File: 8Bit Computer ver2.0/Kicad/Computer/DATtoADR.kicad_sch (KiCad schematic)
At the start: 12 parts, among them IC224 SN74F521DWR, IC225 SN74F521DWR, IC226 SN74F521DWR, IC227 SN74LVC1G14DBVR, IC228 SN74LVC1G14DBVR, IC229 SN74LVC1G14DBVR, IC230 SN74LVC1G14DBVR, IC231 SN74ABT574ADWR, IC232 SN74ABT574ADWR, IC233 SN74AHC74DR, IC234 SN74ABT245BDWR, IC235 SN74ABT245BDWR

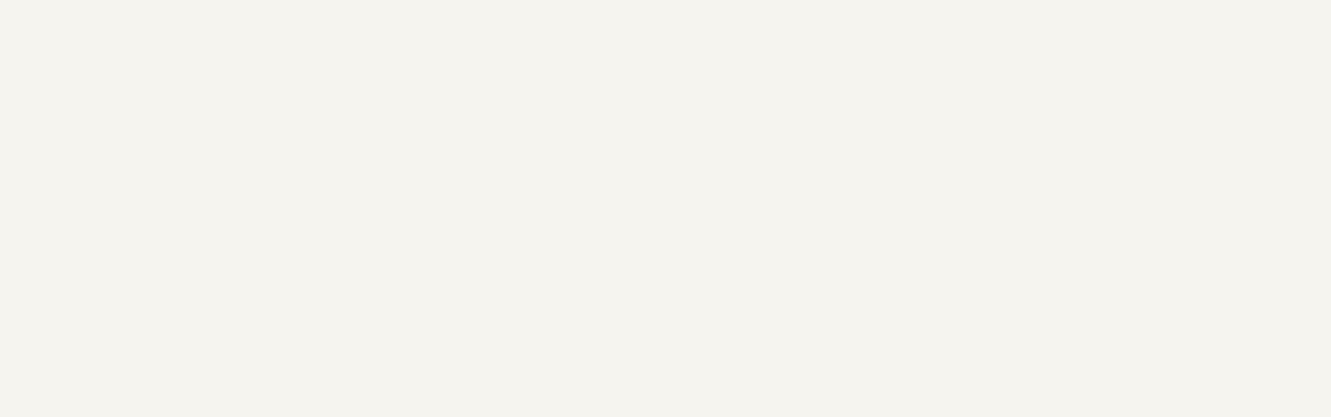
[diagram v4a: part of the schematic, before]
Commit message: Kicad
added the Programme Counter und Dat to adr module
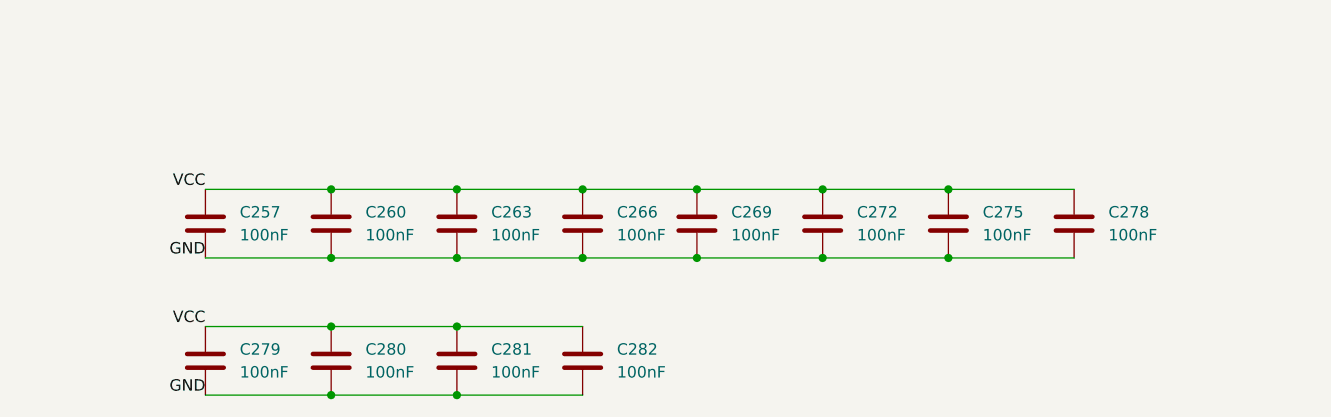
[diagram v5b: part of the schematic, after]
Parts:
- added C257, C260, C263, C266, C269, C272, C275, C278, C279, C280, C281, C282: 100nF, Capacitor_SMD:C_1206_3216Metric_Pad1.33x1.80mm_HandSolder, symbol Device:C
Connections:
- net GND: now also C257.1, C260.1, C263.1, C266.1, C269.1, C272.1, C275.1, C278.1, C279.1, C280.1, C281.1, C282.1
- net VCC: now also C257.2, C260.2, C263.2, C266.2, C269.2, C272.2, C275.2, C278.2, C279.2, C280.2, C281.2, C282.2

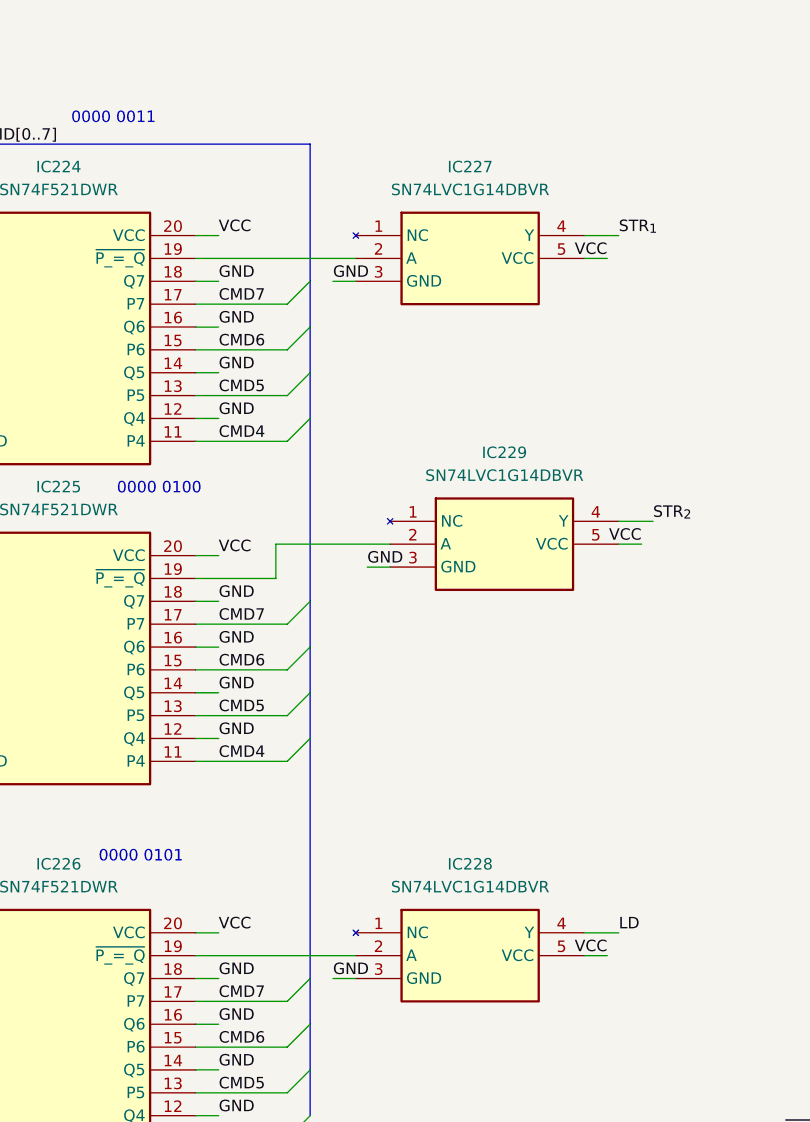
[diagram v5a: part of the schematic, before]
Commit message: Kicad
added 10pin 2,54mm Header
finished ALU PCB and added pin Header for extra use (DAT,ADR,CMD,Ddis,CLK)
31.12-06.01 about +60hr for ALU
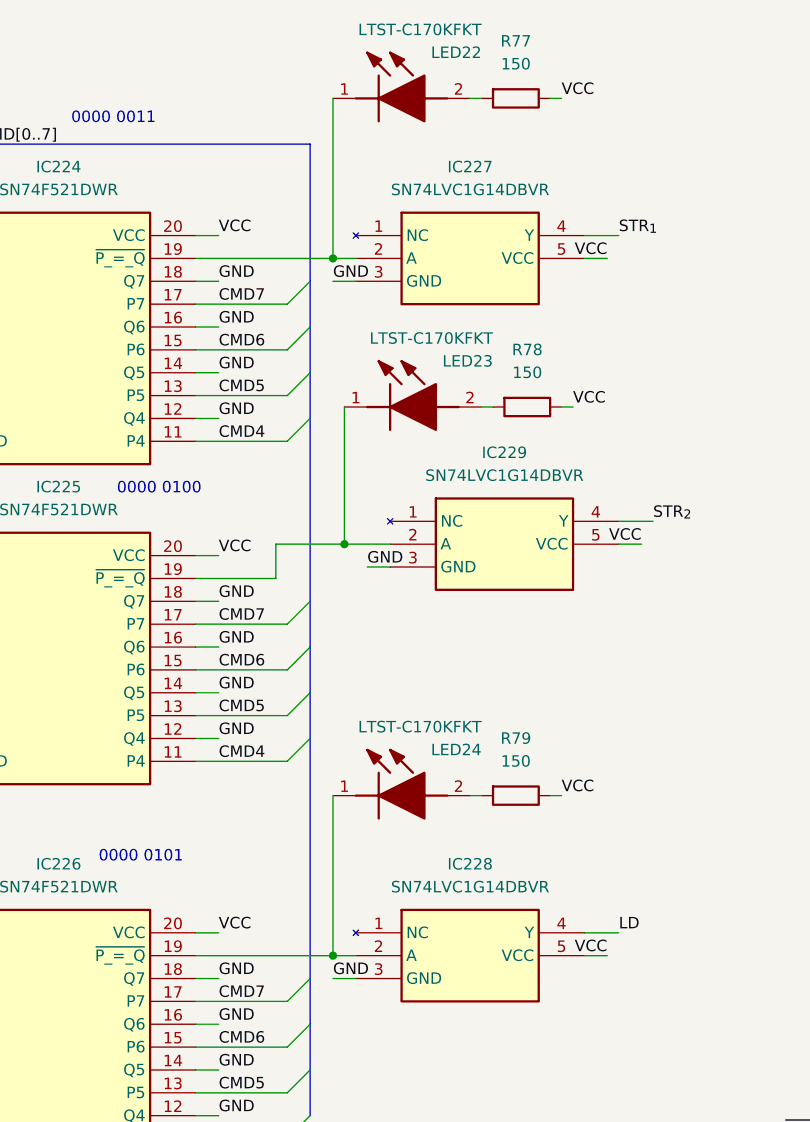
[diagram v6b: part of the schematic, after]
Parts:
- added LED22, LED23, LED24: LTST-C170KFKT, Samacsys:LEDC2012X120N, symbol Samacsys:LTST-C170KFKT
- added R77, R78, R79: 150, Resistor_SMD:R_1206_3216Metric_Pad1.30x1.75mm_HandSolder, symbol Device:R
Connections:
- net VCC: now also R77.1, R78.1, R79.1
- net at IC224.19 (~{P_=_Q}), IC227.2 (A): now also LED22.1 (K)
- net at IC226.19 (~{P_=_Q}), IC228.2 (A): now also LED24.1 (K)
- net at IC225.19 (~{P_=_Q}), IC229.2 (A): now also LED23.1 (K)
- new net: LED23.2 (A), R78.2
- new net: LED24.2 (A), R79.2
- new net: LED22.2 (A), R77.2

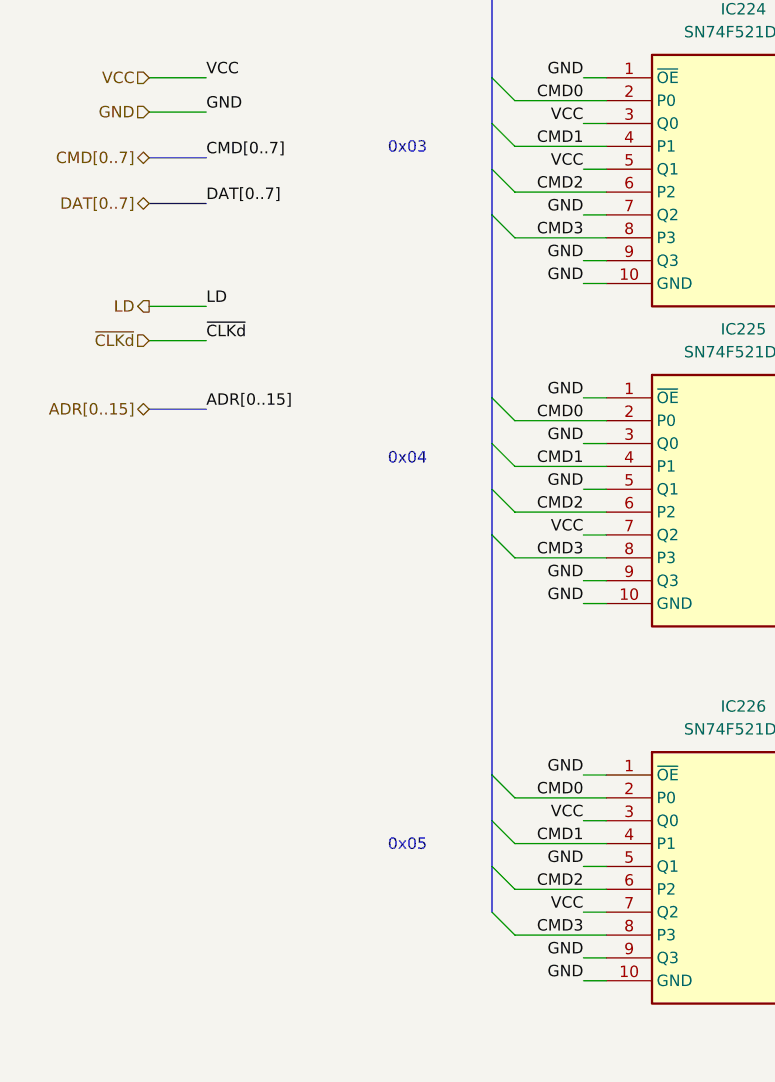
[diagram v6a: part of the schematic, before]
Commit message: Kicad
fixed some design errors(dat dis DistShiftreg, wrong cmd pins)
added description to every CMD for better debug, use CTRL+f and use option "Whole words only" to search e.g. inc
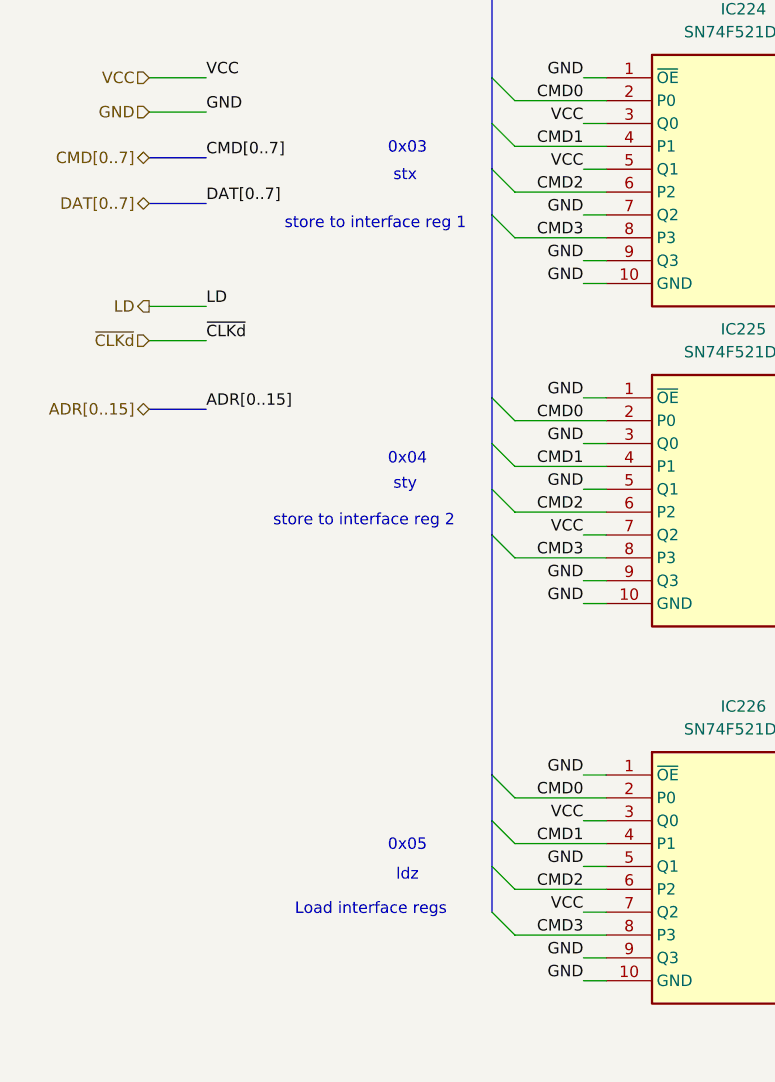
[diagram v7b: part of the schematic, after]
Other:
- note added: "Load interface regs"
- note added: "ldz"
- note added: "store to interface reg 1"
- note added: "store to interface reg 2"
- note added: "stx"
- note added: "sty"
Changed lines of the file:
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@@
+		)
+	)
+	(text "sty"
+		(exclude_from_sim no)
+		(at 64.008 83.312 0)
+		(effects
+			(font
+				(size 1.27 1.27)
+			)
+		)
+	)
+	(text "ldz"
+		(exclude_from_sim no)
+		(at 64.262 126.746 0)
+		(effects
+			(font
+				(size 1.27 1.27)
+			)
 		)
 	)
@@
 		(exclude_from_sim no)
 		(at 112.776 66.294 0)
+		(effects
+			(font
+				(size 1.27 1.27)
+			)
+		)
+	)
+	(text "stx"
+		(exclude_from_sim no)
+		(at 64.008 49.022 0)
 		(effects
 			(font
@@
 		)
 	)
+	(text "store to interface reg 2"
+		(exclude_from_sim no)
+		(at 59.436 87.376 0)
+		(effects
+			(font
+				(size 1.27 1.27)
+			)
+		)
+	)
+	(text "store to interface reg 1"
+		(exclude_from_sim no)
+		(at 60.706 54.356 0)
+		(effects
+			(font
+				(size 1.27 1.27)
+			)
+		)
+	)
 	(text "0x03\n\n"
 		(exclude_from_sim no)
@@
 		(effects
 			(font
+				(size 1.27 1.27)
+			)
+		)
+	)
+	(text "Load interface regs"
+		(exclude_from_sim no)
+		(at 60.198 130.556 0)
+		(effects
+			(font

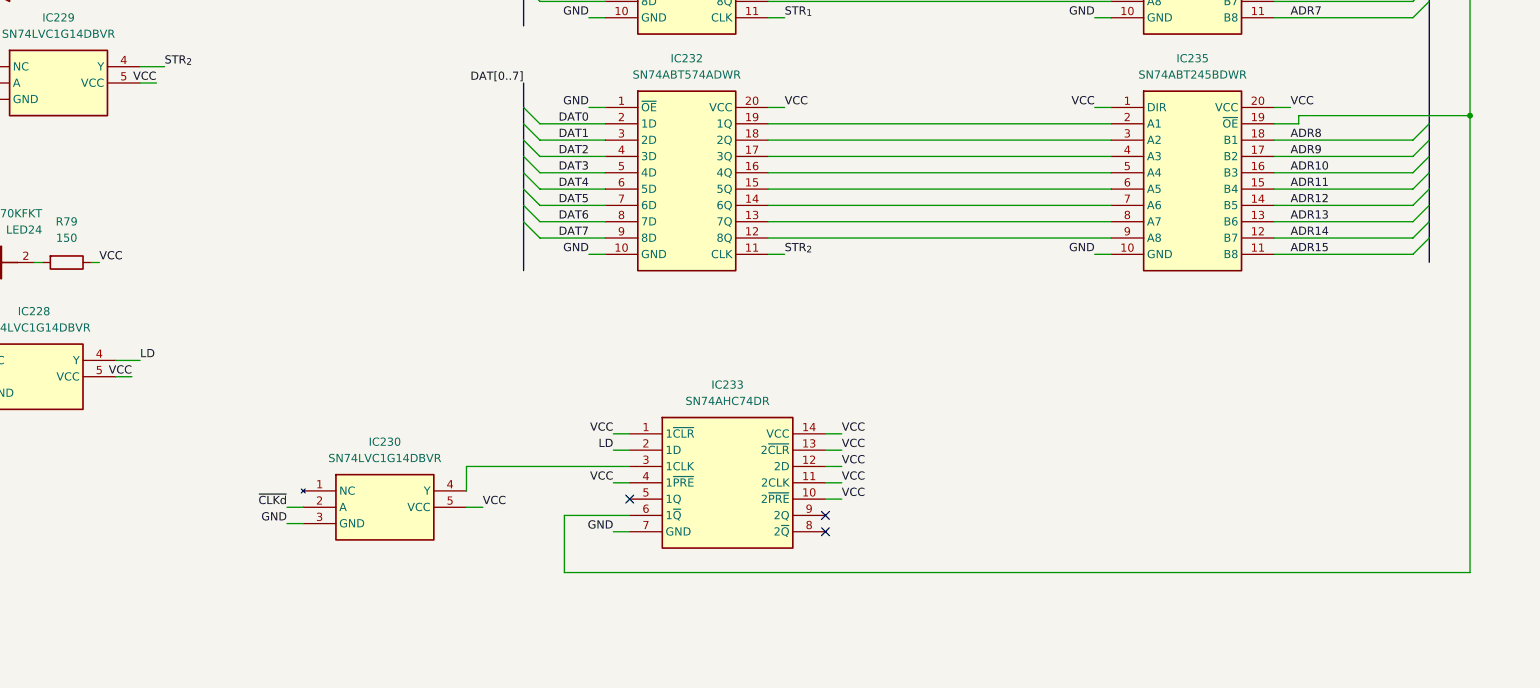
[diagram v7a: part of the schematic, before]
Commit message: fixes
fixed timing for dat to adr register
added a new short test programme for dat to adr register
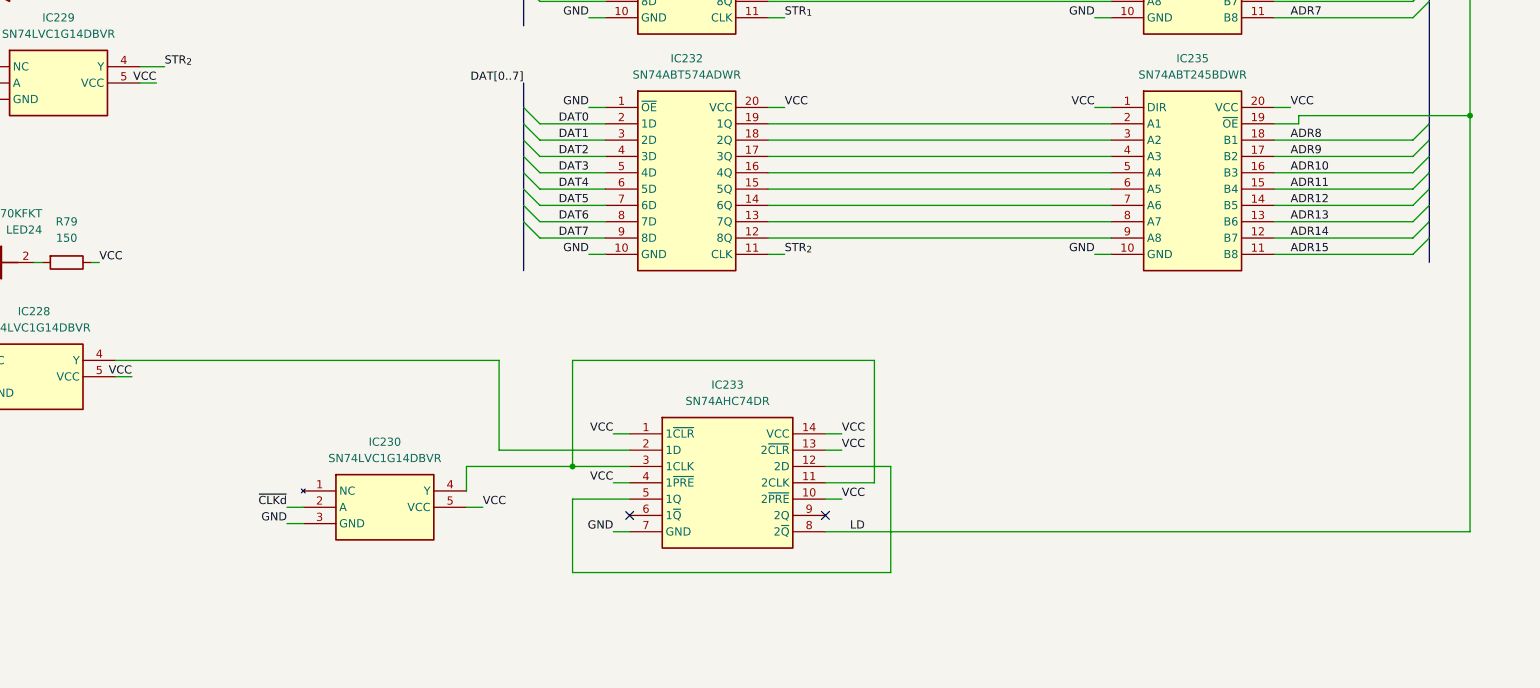
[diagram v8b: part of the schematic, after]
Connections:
- net LD: now also IC233.8 (2~{Q}), IC234.19 (~{OE}), IC235.19 (~{OE}); no longer IC228.4 (Y), IC233.2 (1D)
- net VCC: no longer IC233.11 (2CLK), IC233.12 (2D)
- net at IC230.4 (Y), IC233.3 (1CLK): now also IC233.11 (2CLK)
- net at IC233.5 (1Q): now also IC233.12 (2D)
- new net: IC228.4 (Y), IC233.2 (1D)
- now unconnected: IC233.6 (1~{Q})
- no-connect marks 3 -> 2
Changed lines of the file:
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@@
 	)
 	(junction
+		(at 231.14 132.08)
+		(diameter 0)
+		(color 0 0 0 0)
+	)
+	(junction
 		(at 199.39 179.07)
 		(diameter 0)
@@
 	)
 	(no_connect
-		(at 270.51 139.7)
-	)
-	(no_connect
-		(at 240.03 137.16)
+		(at 240.03 139.7)
 	)
 	(no_connect
-		(at 270.51 142.24)
+		(at 270.51 139.7)
 	)
 	(bus_entry
@@
 	(wire
 		(pts
+			(xy 278.13 134.62) (xy 278.13 115.57)
+		)
+		(stroke
+			(width 0)
+			(type default)
+		)
+	)
+	(wire
+		(pts
 			(xy 340.36 83.82) (xy 361.95 83.82)
 		)
@@
 	(wire
 		(pts
-			(xy 160.02 115.57) (xy 163.83 115.57)
-		)
-		(stroke
-			(width 0)
-			(type default)
-		)
-	)
-	(wire
-		(pts
 			(xy 119.38 120.65) (xy 116.84 120.65)
 		)
@@
 		)
 	)
-	(wire
-		(pts
-			(xy 237.49 129.54) (xy 240.03 129.54)
-		)
-		(stroke
-			(width 0)
-			(type default)
-		)
-	)
 	(bus
 		(pts
@@
 	(wire
 		(pts
-			(xy 370.84 148.59) (xy 370.84 77.47)
+			(xy 370.84 142.24) (xy 370.84 77.47)
 		)
 		(stroke
@@
 	(wire
 		(pts
-			(xy 270.51 134.62) (xy 273.05 134.62)
+			(xy 270.51 134.62) (xy 278.13 134.62)
 		)
 		(stroke
@@
 	(wire
 		(pts
-			(xy 229.87 139.7) (xy 229.87 148.59)
-		)
-		(stroke
-			(width 0)
-			(type default)
-		)
-	)
-	(wire
-		(pts
 			(xy 76.2 123.19) (xy 86.36 123.19)
 		)
@@
 	(wire
 		(pts
+			(xy 278.13 115.57) (xy 231.14 115.57)
+		)
+		(stroke
+			(width 0)
+			(type default)
+		)
+	)
+	(wire
+		(pts
 			(xy 158.75 171.45) (xy 172.72 171.45)
 		)
@@
 	(wire
 		(pts
-			(xy 214.63 132.08) (xy 240.03 132.08)
+			(xy 214.63 132.08) (xy 231.14 132.08)
 		)
 		(stroke
@@
 	(wire
 		(pts
+			(xy 270.51 142.24) (xy 370.84 142.24)
+		)
+		(stroke
+			(width 0)
+			(type default)
+		)
+	)
+	(wire
+		(pts
 			(xy 199.39 179.07) (xy 213.36 179.07)
 		)
@@
 	(wire
 		(pts
+			(xy 160.02 115.57) (xy 219.71 115.57)
+		)
+		(stroke
+			(width 0)
+			(type default)
+		)
+	)
+	(wire
+		(pts
 			(xy 261.62 54.61) (xy 314.96 54.61)
 		)
@@
 		)
 	)
+	(wire
+		(pts
+			(xy 231.14 132.08) (xy 240.03 132.08)
+		)
+		(stroke
+			(width 0)
+			(type default)
+		)
+	)
 	(bus
 		(pts
@@
 	(wire
 		(pts
+			(xy 231.14 115.57) (xy 231.14 132.08)
+		)
+		(stroke
+			(width 0)
+			(type default)
+		)
+	)
+	(wire
+		(pts
 			(xy 148.59 100.33) (xy 147.32 100.33)
 		)
@@
 	(wire
 		(pts
+			(xy 219.71 129.54) (xy 219.71 115.57)
+		)
+		(stroke
+			(width 0)
+			(type default)
+		)
+	)
+	(wire
+		(pts
 			(xy 158.75 186.69) (xy 172.72 186.69)
 		)
@@
 		)
 	)
+	(wire
+		(pts
+			(xy 280.67 132.08) (xy 270.51 132.08)
+		)
+		(stroke
+			(width 0)
+			(type default)
+		)
+	)
 	(bus
 		(pts
@@
 	(wire
 		(pts
-			(xy 240.03 139.7) (xy 229.87 139.7)
-		)
-		(stroke
-			(width 0)
-			(type default)
-		)
-	)
-	(wire
-		(pts
 			(xy 156.21 22.86) (xy 157.48 22.86)
 		)
@@
 		)
 	)
-	(wire
-		(pts
-			(xy 270.51 132.08) (xy 273.05 132.08)
-		)
-		(stroke
-			(width 0)
-			(type default)
-		)
-	)
 	(bus
 		(pts
@@
 		)
 	)
-	(bus
+	(wire
 		(pts
-			(xy 223.52 54.61) (xy 223.52 57.15)
+			(xy 240.03 137.16) (xy 231.14 137.16)
 		)
 		(stroke
@@
 		)
 	)
-	(wire
+	(bus
 		(pts
-			(xy 229.87 148.59) (xy 370.84 148.59)
+			(xy 223.52 54.61) (xy 223.52 57.15)
 		)
 		(stroke
@@
 	(wire
 		(pts
+			(xy 280.67 148.59) (xy 280.67 132.08)
+		)
+		(stroke
+			(width 0)
+			(type default)
+		)
+	)
+	(wire
+		(pts
 			(xy 119.38 58.42) (xy 116.84 58.42)
 		)
@@
 	(wire
 		(pts
+			(xy 231.14 148.59) (xy 280.67 148.59)
+		)
+		(stroke
+			(width 0)
+			(type default)
+		)
+	)
+	(wire
+		(pts
 			(xy 144.78 179.07) (xy 158.75 179.07)
 		)
@@
 	(wire
 		(pts
+			(xy 219.71 129.54) (xy 240.03 129.54)
+		)
+		(stroke
+			(width 0)
+			(type default)
+		)
+	)
+	(wire
+		(pts
 			(xy 226.06 96.52) (xy 236.22 96.52)
 		)
@@
 		)
 	)
+	(wire
+		(pts
+			(xy 231.14 137.16) (xy 231.14 148.59)
+		)
+		(stroke
+			(width 0)
+			(type default)
+		)
+	)
 	(bus
 		(pts
@@
 		)
 	)
-	(label "VCC"
-		(at 273.05 132.08 0)
-		(effects
-			(font
-				(size 1.27 1.27)
-			)
-			(justify left bottom)
-		)
-	)
 	(label "GND"
 		(at 83.82 135.89 180)
@@
 		)
 	)
-	(label "VCC"
-		(at 273.05 134.62 0)
-		(effects
-			(font
-				(size 1.27 1.27)
-			)
-			(justify left bottom)
-		)
-	)
 	(label "DAT4"
 		(at 233.68 52.07 180)
@@
 		)
 	)
-	(label "LD"
-		(at 237.49 129.54 180)
-		(effects
-			(font
-				(size 1.27 1.27)
-			)
-			(justify right bottom)
-		)
-	)
 	(label "CMD2"
 		(at 83.82 128.27 180)
@@
 		)
 	)
-	(label "LD"
-		(at 163.83 115.57 0)
-		(effects
-			(font
-				(size 1.27 1.27)
-			)
-			(justify left bottom)
-		)
-	)
 	(label "VCC"
 		(at 166.37 72.39 180)
@@
 		)
 	)
+	(label "LD"
+		(at 274.32 142.24 0)
+		(effects
+			(font
+				(size 1.27 1.27)
+			)
+			(justify left bottom)
+		)
+	)
